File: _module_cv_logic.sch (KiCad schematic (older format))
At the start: 29 parts, among them J15 conn_L, J16 conn_R, J17 power_bus, U1 4017, U2 TL074, U3 4013

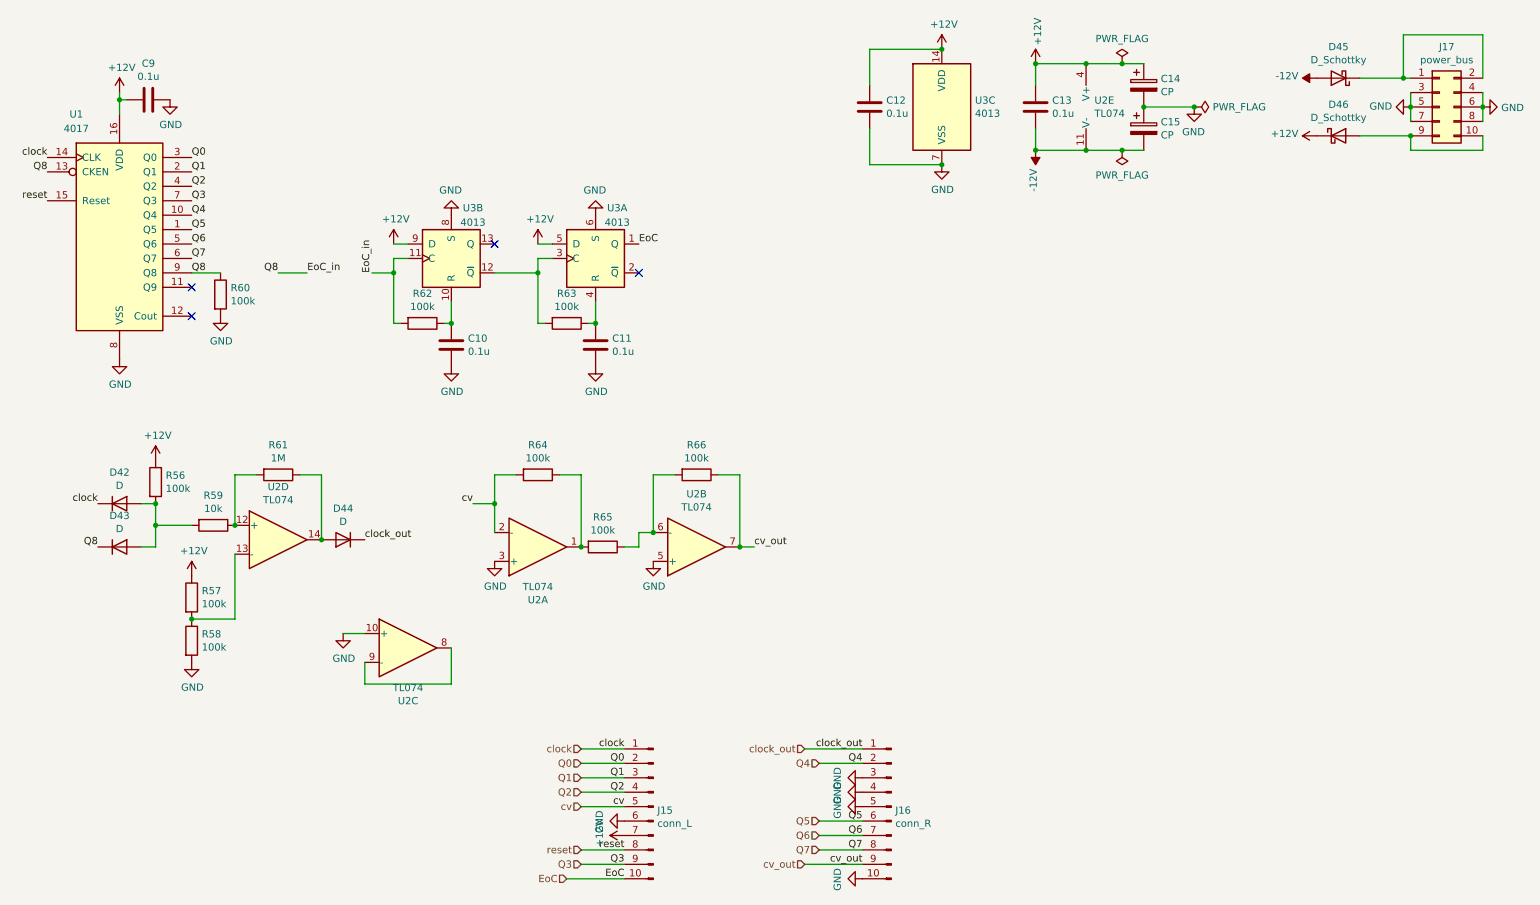
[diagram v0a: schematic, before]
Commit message: Fixed problems: - added power-on reset function - added 100ks to discharge caps with FFs(4013) - only for the CV; adjusted the parameter (100k -> 10k) of a resistor with a FF
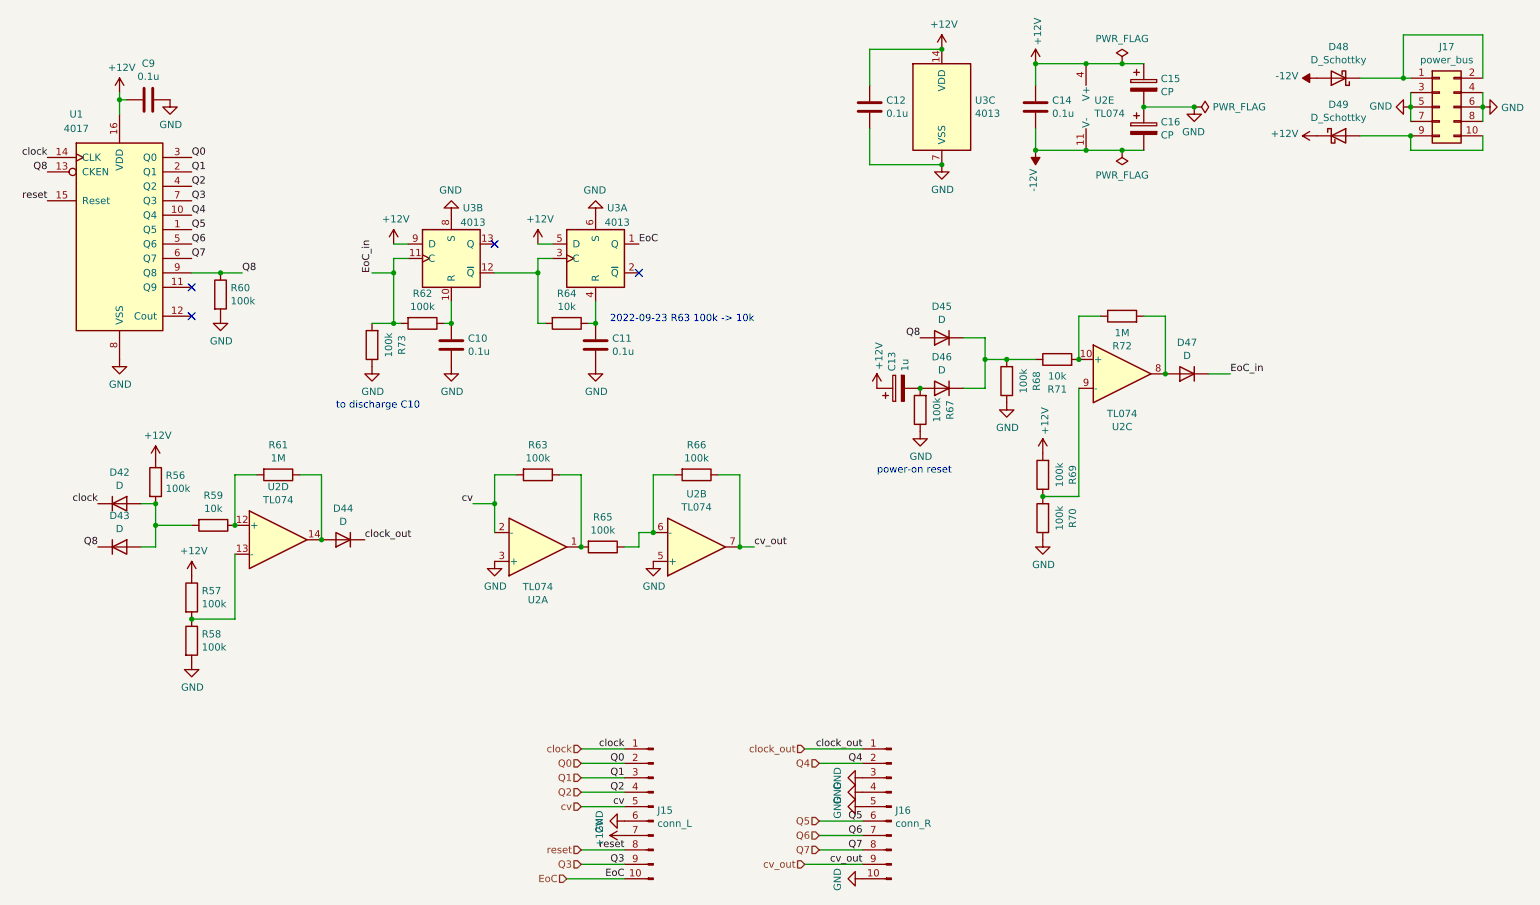
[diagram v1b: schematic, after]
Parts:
- added C13: 1u, Capacitor_THT:CP_Radial_D5.0mm_P2.50mm, symbol Device:CP
- added D45, D46, D47: D, Diode_THT:D_DO-34_SOD68_P2.54mm_Vertical_AnodeUp, symbol Device:D
- added R67, R68, R69, R70, R73: 100k, Resistor_THT:R_Axial_DIN0207_L6.3mm_D2.5mm_P2.54mm_Vertical, symbol Device:R
- added R71: 10k, Resistor_THT:R_Axial_DIN0207_L6.3mm_D2.5mm_P7.62mm_Horizontal, symbol Device:R
- added R72: 1M, Resistor_THT:R_Axial_DIN0207_L6.3mm_D2.5mm_P2.54mm_Vertical, symbol Device:R
- R64: renamed from R63; value 100k -> 10k
- renumbered C13 to C14, C14 to C15, C15 to C16, D45 to D48, D46 to D49, R64 to R63
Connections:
- net +12V: now also C13.1, R69.2
- net EoC_in: now also D47.1 (K), R73.2; no longer D43.1 (K), R60.1, U1.13 (CKEN), U1.9 (Q8)
- net GND: now also R67.1, R68.1, R70.1, R73.1; no longer U2.10 (+)
- net at U2.8: now also D47.2 (A), R72.2; no longer U2.9 (-)
- new net: R71.2, R72.1, U2.10 (+)
- new net: R69.1, R70.2, U2.9 (-)
- new net: D45.1 (K), D46.1 (K), R68.2, R71.1
- new net: C13.2, D46.2 (A), R67.2
- new net Q8: D43.1 (K), D45.2 (A), R60.1, U1.13 (CKEN), U1.9 (Q8)
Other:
- note added: "2022-09-23 R63 100k -> 10k"
- note added: "power-on reset"
- note added: "to discharge C10"
- moved on the sheet: U2C
